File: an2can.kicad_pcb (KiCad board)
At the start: 2 copper layers, 67.7 x 49.8 mm, 142 parts, among them J1 PWR/CAN, J2 USB C, J3 DBG, J4 5V IN, J5 Input, J6 Aux, J7 Input, J8 Input, J9 Input, Q1 PMV65XP, SW1 RESET, U1 MAX6025, U10 AD8221ARZ, U11 Opamp_Dual, U12 AD8221ARZ, U13 Opamp_Dual, U2 Tex_DCDC_v2, U3 DSC61XX, U4 STM32L432KCUx, U5 MCP2562FD, U6 AD8221ARZ, U7 Opamp_Dual, U8 AD8221ARZ, U9 Opamp_Dual

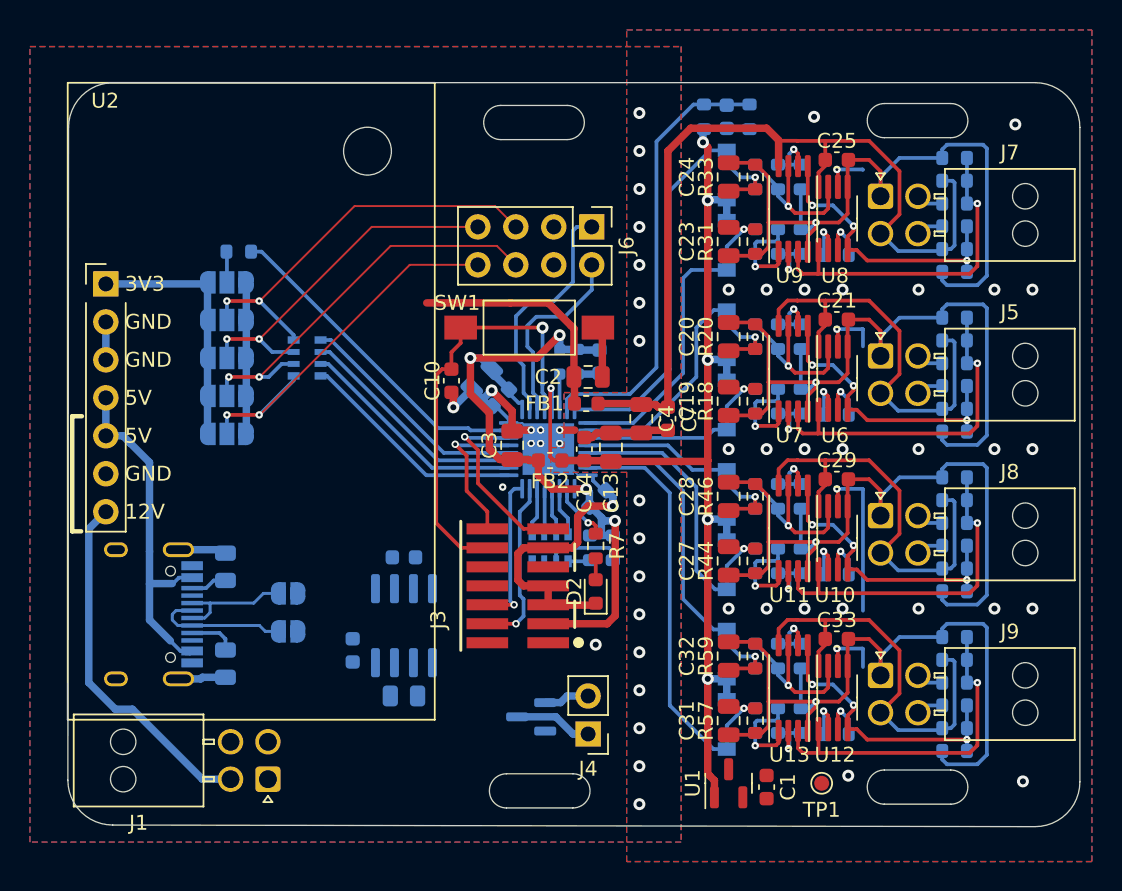
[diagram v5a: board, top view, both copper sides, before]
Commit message: pcb: complete routing, add silkscreen details, finalize board
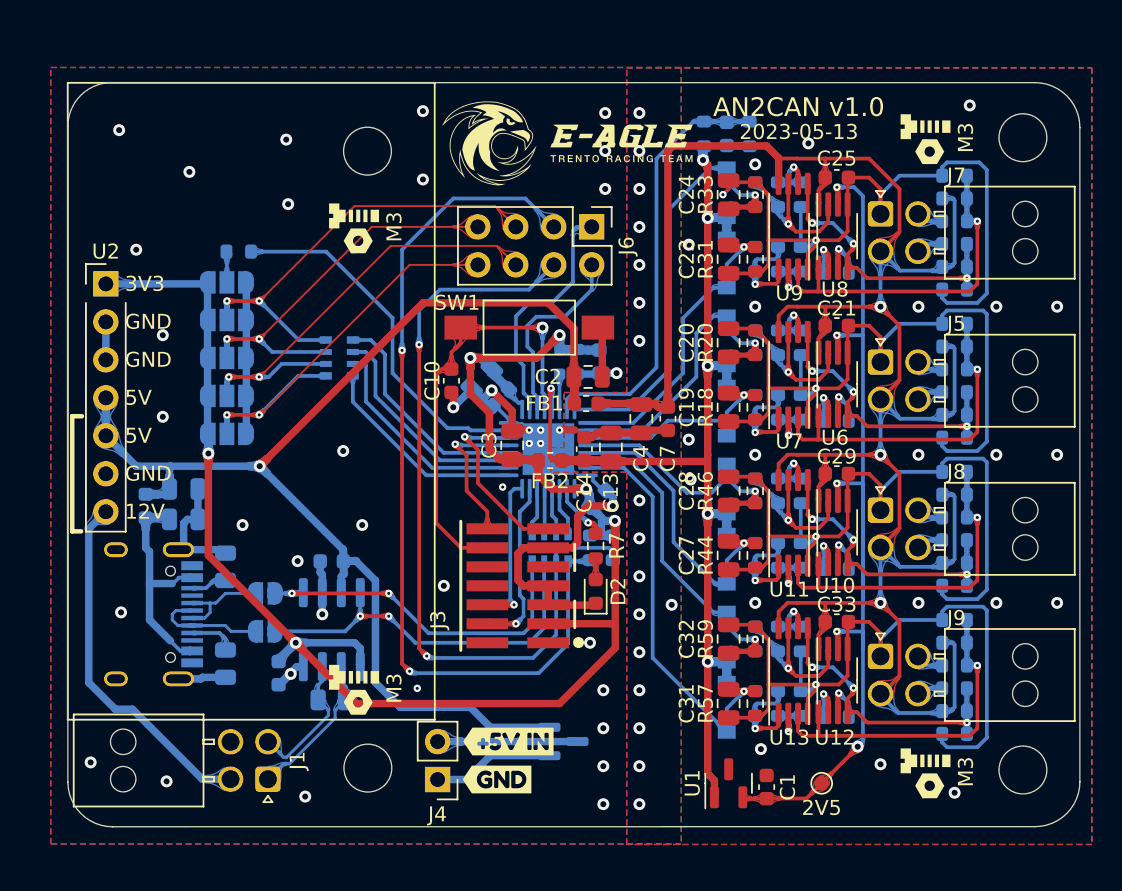
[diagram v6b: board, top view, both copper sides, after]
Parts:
- added C5: C, Capacitor_SMD:C_0805_2012Metric, B.Cu at (70.0, 95.1)
- added C8: C, Capacitor_SMD:C_0805_2012Metric, B.Cu at (70.0, 93.1)
- added FB3: FerriteBead, Inductor_SMD:L_0603_1608Metric, B.Cu at (67.4, 94.2)
- added G***: LOGO, LOGO, F.Cu at (81.3, 75.6)
- added G***: LOGO, LOGO, F.Cu at (95.6, 70.0)
- added G***: LOGO, LOGO, F.Cu at (119.5, 112.0)
- added G***: LOGO, LOGO, F.Cu at (119.5, 69.6)
- added G***: LOGO, LOGO, F.Cu at (81.3, 106.4)
- added G***: LOGO, LOGO, B.Cu at (93.0, 103.6)
- added H1: MountingHole, Eagle_Main:MountingHole_3.2mm_M3_ISO14580, F.Cu at (82.3, 111.8)
- added H2: MountingHole, Eagle_Main:MountingHole_3.2mm_M3_ISO14580, F.Cu at (126.1, 69.6)
- added H3: MountingHole, Eagle_Main:MountingHole_3.2mm_M3_ISO14580, F.Cu at (126.1, 111.9)
- added kibuzzard-645FEBDB: G***, kibuzzard-645FEBDB, F.Cu at (91.7, 110.0)
- added kibuzzard-645FEBF3: G***, kibuzzard-645FEBF3, F.Cu at (90.9, 112.5)
- moved J4 10.5 mm to (87.0, 112.5)
- moved C16 5.18 mm to (76.3, 105.4)
- moved C17 4.83 mm to (79.9, 97.9)
- moved R6 4.83 mm to (79.9, 107.2)
- moved U5 4.83 mm to (79.9, 102.5)
- moved Q1 2.72 mm to (95.4, 110.0), turned to 0 degrees
- moved RN1 2.16 mm to (80.4, 84.3)
- moved JP6 1.52 mm to (75.4, 102.6)
- moved JP7 1.52 mm to (75.4, 100.1)
- moved J9 1.27 mm to (116.6, 104.3)
- moved C24 1.18 mm to (106.4, 73.4)
- moved C25 1.18 mm to (113.7, 72.3)
- moved R27 1.18 mm to (111.3, 73.4)
- moved R29 1.18 mm to (109.7, 73.4)
- moved R32 1.18 mm to (108.2, 73.4)
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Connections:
- J1 pad 1: /CAN+ -> /CAN-
- J1 pad 2: /CAN- -> /CAN+
- J2 pad A4: +5V -> /MCU/+5V_USB_UNFILTERED
- J2 pad A9: +5V -> /MCU/+5V_USB_UNFILTERED
- J2 pad B4: +5V -> /MCU/+5V_USB_UNFILTERED
- J2 pad B9: +5V -> /MCU/+5V_USB_UNFILTERED
- J4 pad 1: Net-(J4-Pad1) -> GND
- J4 pad 2: GND -> Net-(Q1-Pad3)
- Q1 pad 3: Net-(J4-Pad1) -> Net-(Q1-Pad3)
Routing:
- net /MCU/I2C_SCL: track 1.50 -> 59.1 mm, vias 0 -> 2
- net +3V3: track 64.7 -> 114.2 mm, vias 4 -> 6
- net /MCU/I2C_SDA: track 5.16 -> 53.0 mm, vias 0 -> 2
- net /2V5_OFFSET: track 22.3 -> 67.3 mm, vias 4 -> 5
- net +5V: track 39.6 -> 81.4 mm, vias 0 -> 1
- net /MCU/CAN_RX: track 0.00 -> 25.6 mm, vias 0 -> 2
- net /MCU/CAN_TX: track 0.00 -> 23.5 mm, vias 0 -> 2
- net GND: track 65.5 -> 81.0 mm, vias 11 -> 39
- net /MCU/+5V_USB_UNFILTERED: track 0.00 -> 15.2 mm
- net +5VA: track 147.7 -> 159.3 mm, vias 0 -> 3
- net /CAN-: track 0.00 -> 10.0 mm
- net Net-(Q1-Pad3): track 0.00 -> 9.35 mm
- net /CAN+: track 0.00 -> 9.29 mm
- net Net-(J4-Pad1): track 5.22 -> 0.00 mm
- net /Input Stage 4/OUT_SINGLE: track 31.2 -> 28.7 mm
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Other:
- outline, holes or cut-outs redrawn
- board text added: "+5V IN"
- board text added: "+5VA"
- board text added: "1"
- board text added: "2"
- board text added: "2023-05-13"
- board text added: "2V5"
- board text added: "3"
- board text added: "3V3"
- board text added: "4"
- board text added: "5V"
- board text added: "A0"
- board text added: "A1"
- board text added: "A2"
- board text added: "A3"
- board text added: "AN2CAN v1.0"
- board text added: "BOOT0"
- board text added: "CAN"
- board text added: "CS"
- board text added: "GND"
- board text added: "GNDA"
- board text added: "H"
- board text added: "HIGH | |x|x| LOW |x|x| |"
- board text added: "IN 0"
- board text added: "IN 1"
- board text added: "L"
- board text added: "M3"
- board text added: "MISO"
- board text added: "MOSI"
- board text added: "SCK"
- board text added: "SCL"
- board text added: "SDA"
- board text added: "SP1"
- board text added: "SP2"
- board text added: "USB DATA"
- board text added: "VDC"

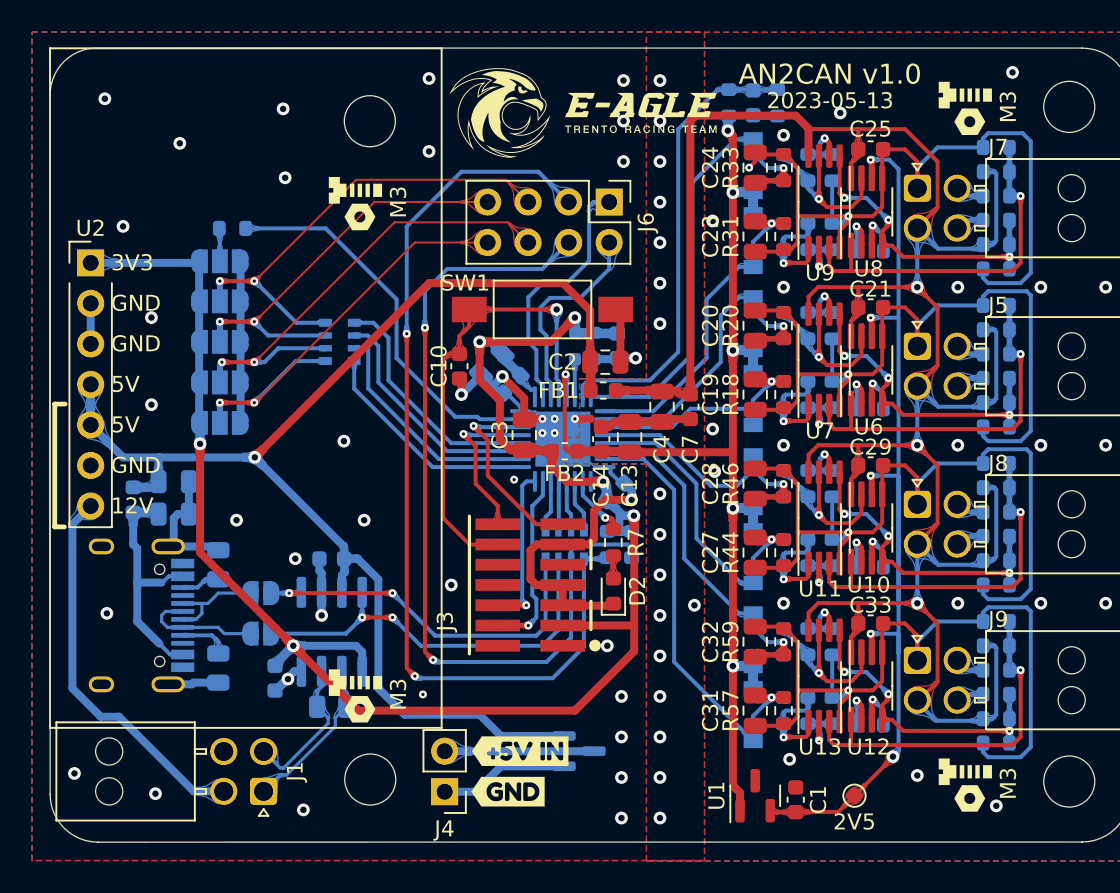
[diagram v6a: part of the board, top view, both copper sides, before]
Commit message: pcb: change oscillator footprint, add board id pad and move board name on back silkscreen
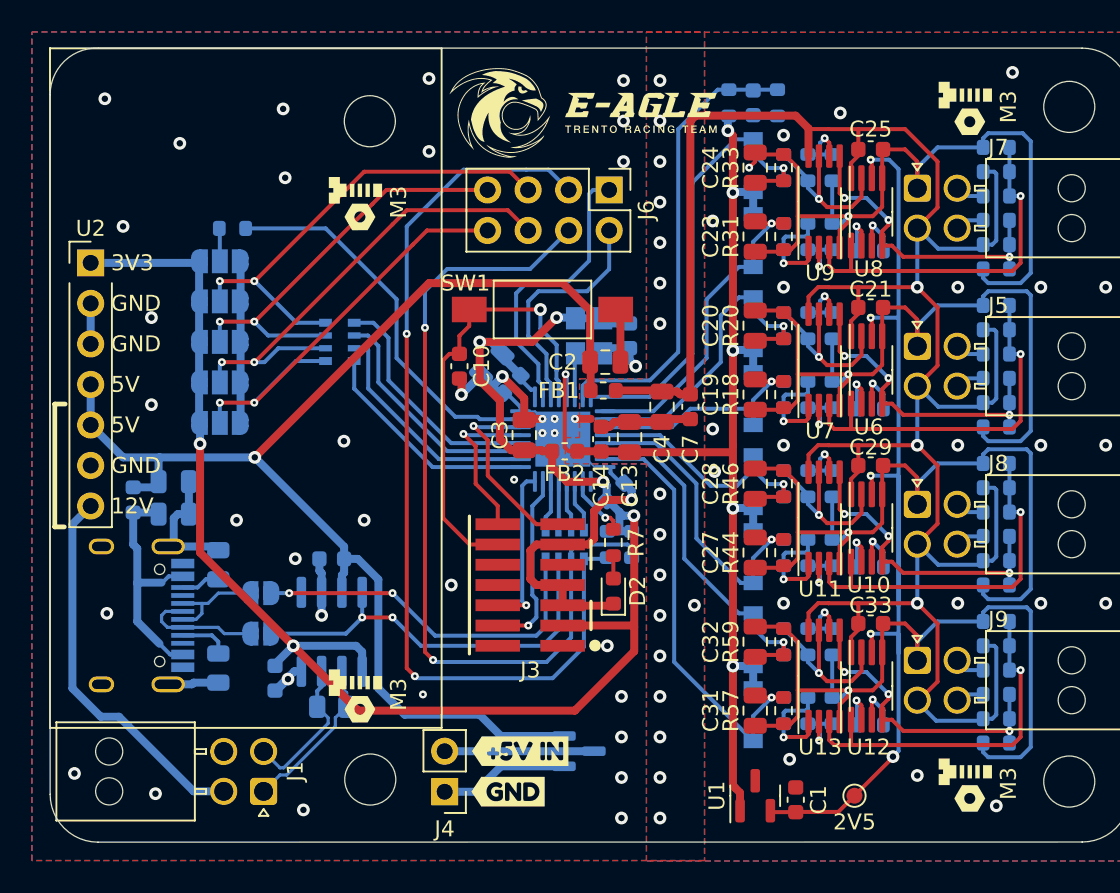
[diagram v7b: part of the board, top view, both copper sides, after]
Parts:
- U3: footprint Package_LGA:VLGA-4_2x2.5mm_P1.65mm -> Crystal:Crystal_SMD_3225-4Pin_3.2x2.5mm
- moved C12 0.99 mm to (98.6, 83.9)
- moved J6 0.76 mm to (97.3, 74.8)
- moved U3 0.68 mm to (96.0, 83.9), turned to -90 degrees
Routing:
- net /MCU/Spare2: track 12.8 -> 14.9 mm
- net /MCU/Spare1: track 16.2 -> 18.2 mm
- net GND: track 81.0 -> 81.6 mm
- net /MCU/~{RESET}: track 29.2 -> 28.7 mm
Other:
- board text added: "2023-05-17 v1.0"
- board text added: "AN2CAN"
- board text added: "Board ID"
- board text removed: "2023-05-13"
- board text removed: "AN2CAN v1.0"

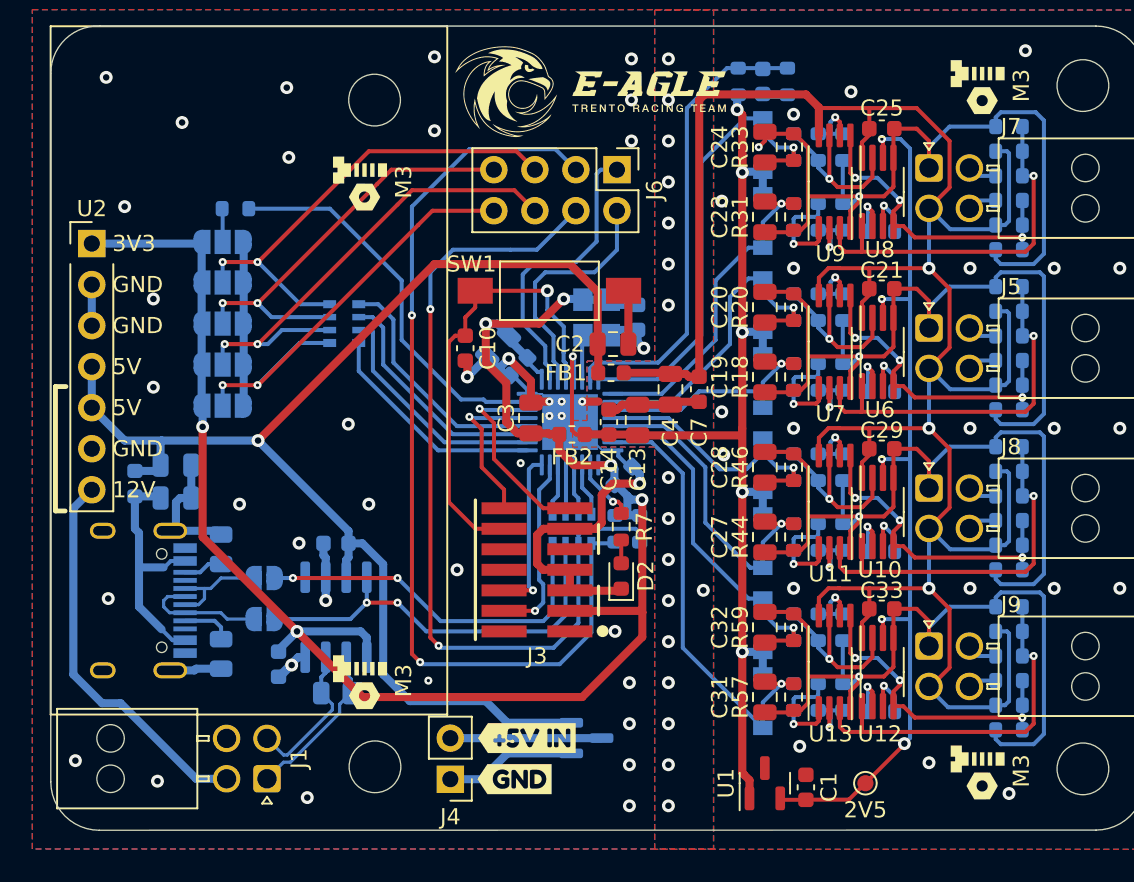
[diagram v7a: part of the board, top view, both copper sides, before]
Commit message: pcb: add teardrops
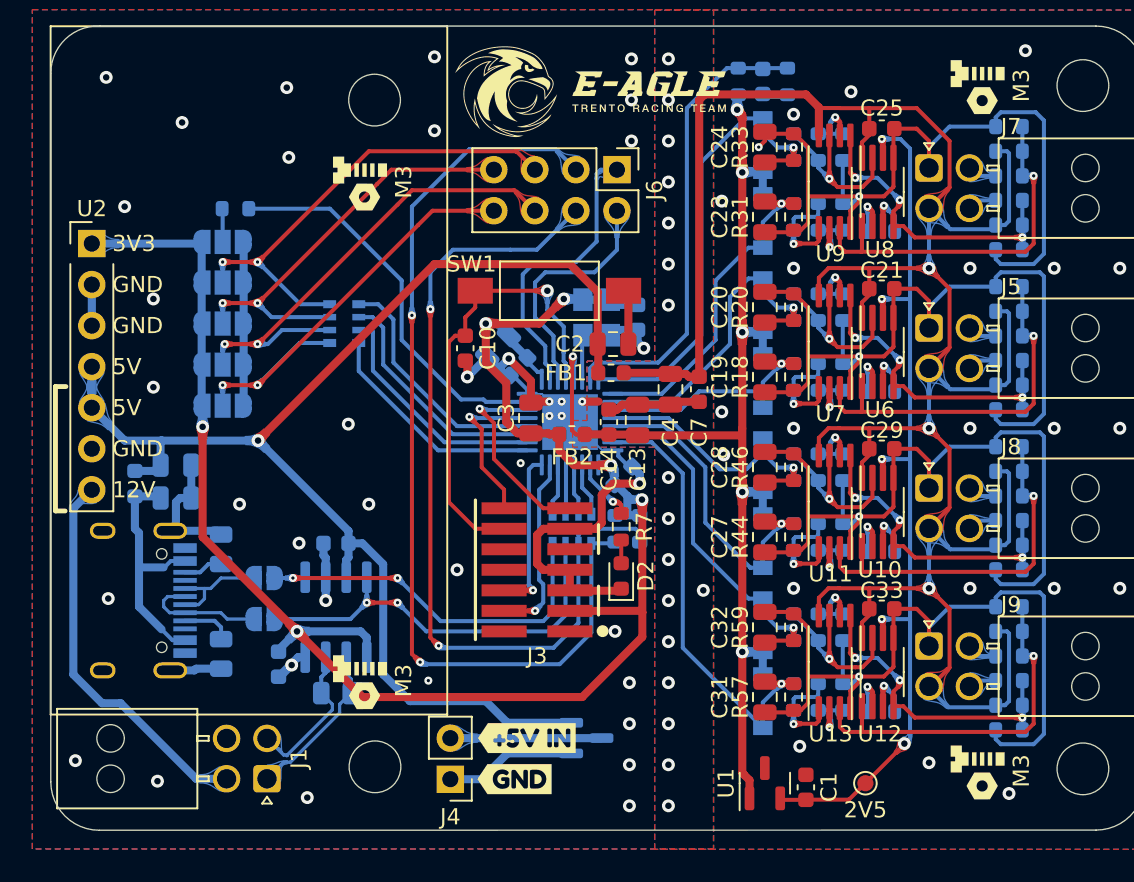
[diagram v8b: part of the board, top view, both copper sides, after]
